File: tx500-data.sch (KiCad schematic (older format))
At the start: 52 parts, among them J1 USB_B_Micro, J2 CAT, J3 REM/DATA, J4 USB_A, U1 TUSB2036, U2 FT232RL, U3 HS-100B, U4 TPS76333, Y1 6MHz

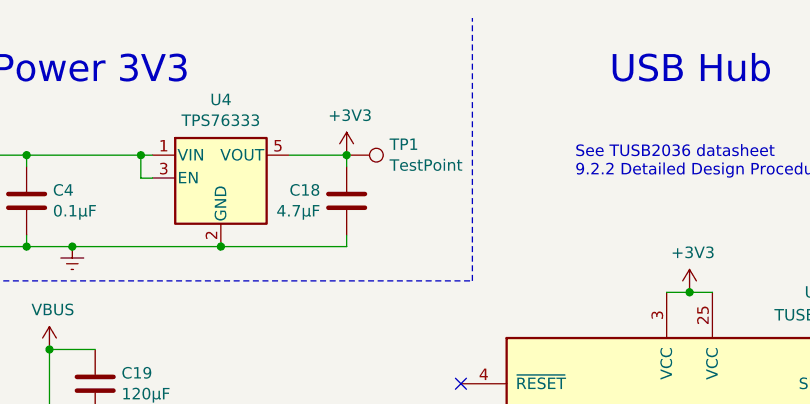
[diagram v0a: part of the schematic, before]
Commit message: Avoid schematic cross-junction
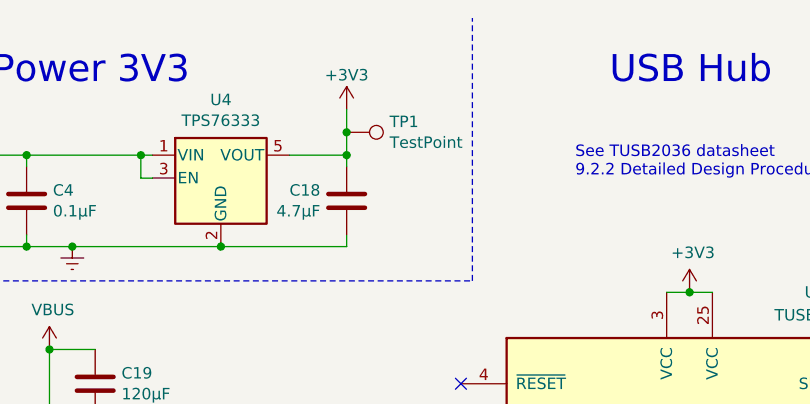
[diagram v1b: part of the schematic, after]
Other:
- moved on the sheet: TP1
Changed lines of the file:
@@
 L power:+3V3 #PWR0110
 U 1 1 60E968EB
-P 2800 1100
-F 0 "#PWR0110" H 2800 950 50  0001 C CNN
-F 1 "+3V3" H 2815 1273 50  0000 C CNN
-F 2 "" H 2800 1100 50  0001 C CNN
-F 3 "" H 2800 1100 50  0001 C CNN
-	1    2800 1100
+P 2800 900
+F 0 "#PWR0110" H 2800 750 50  0001 C CNN
+F 1 "+3V3" H 2800 1050 50  0000 C CNN
+F 2 "" H 2800 900 50  0001 C CNN
+F 3 "" H 2800 900 50  0001 C CNN
+	1    2800 900
 	1    0    0    -1
 $EndComp
@@
 L Connector:TestPoint TP1
 U 1 1 607EF82B
-P 2800 1100
-F 0 "TP1" V 2754 1288 50  0000 L CNN
-F 1 "TestPoint" V 2845 1288 50  0000 L CNN
-F 2 "TestPoint:TestPoint_Pad_D1.0mm" H 3000 1100 50  0001 C CNN
-F 3 "~" H 3000 1100 50  0001 C CNN
-	1    2800 1100
+P 2800 1000
+F 0 "TP1" V 2754 1188 50  0000 L CNN
+F 1 "TestPoint" V 2845 1188 50  0000 L CNN
+F 2 "TestPoint:TestPoint_Pad_D1.0mm" H 3000 1000 50  0001 C CNN
+F 3 "~" H 3000 1000 50  0001 C CNN
+	1    2800 1000
 	0    1    1    0
 $EndComp
@@
 $EndComp
 NoConn ~ 7900 5500
+Wire Wire Line
+	2800 1100 2800 1000
+Connection ~ 2800 1000
+Wire Wire Line
+	2800 1000 2800 900
 $EndSCHEMATC

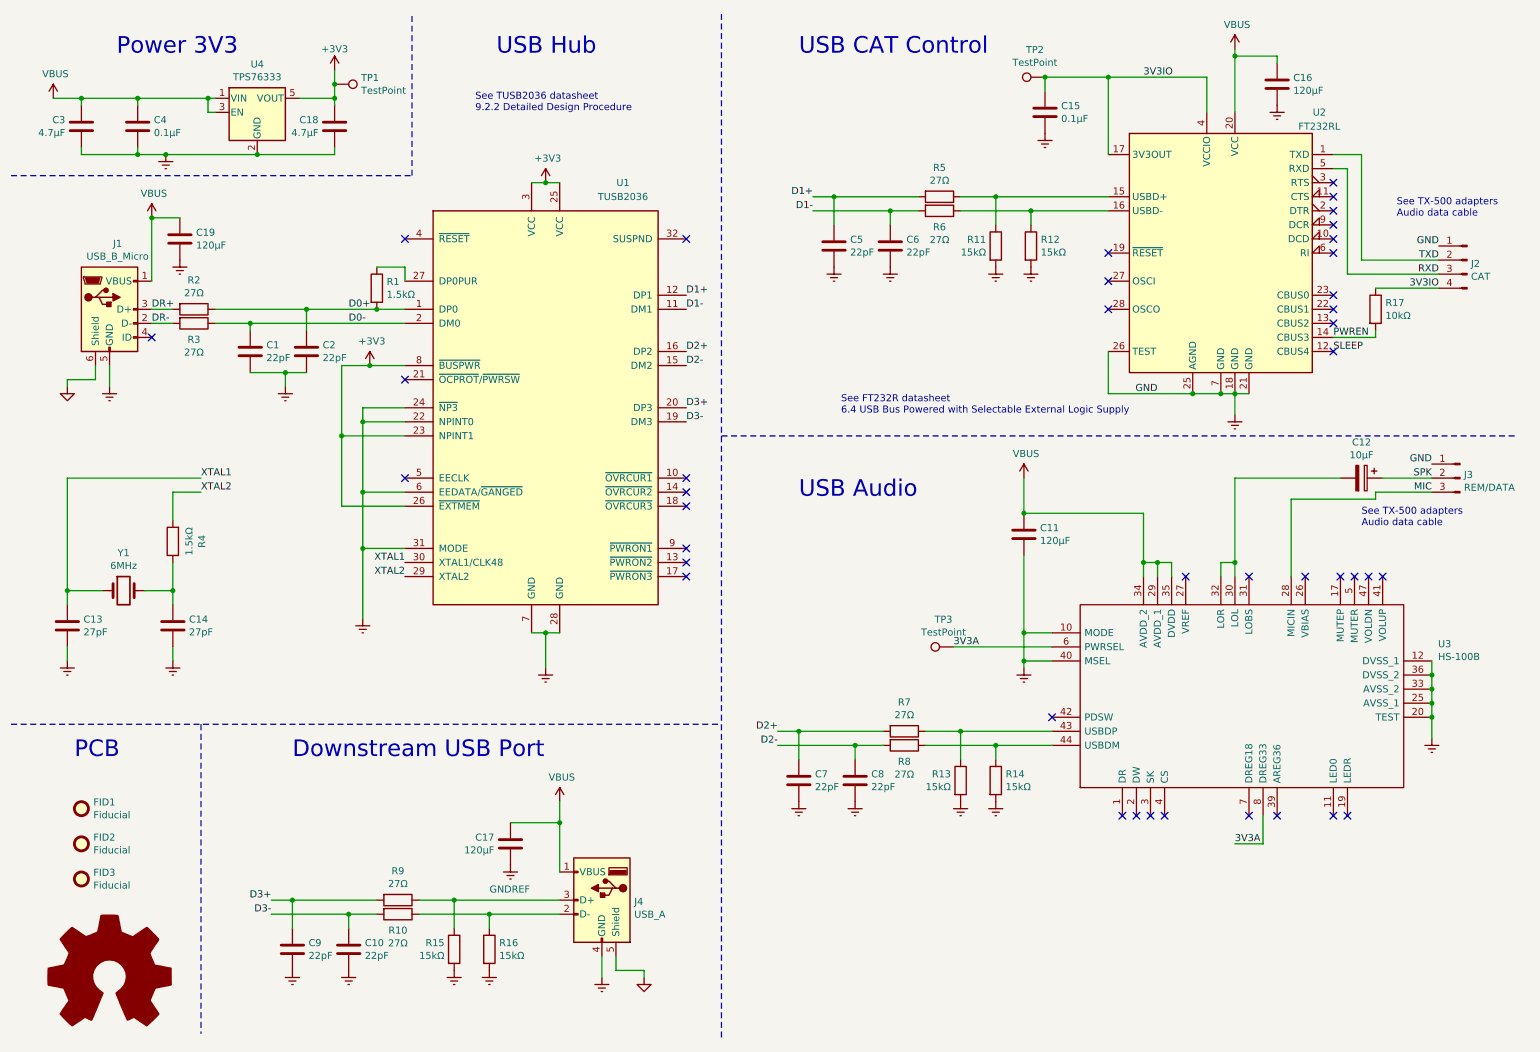
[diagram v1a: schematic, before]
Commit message: Add ESD and overcurrent protection
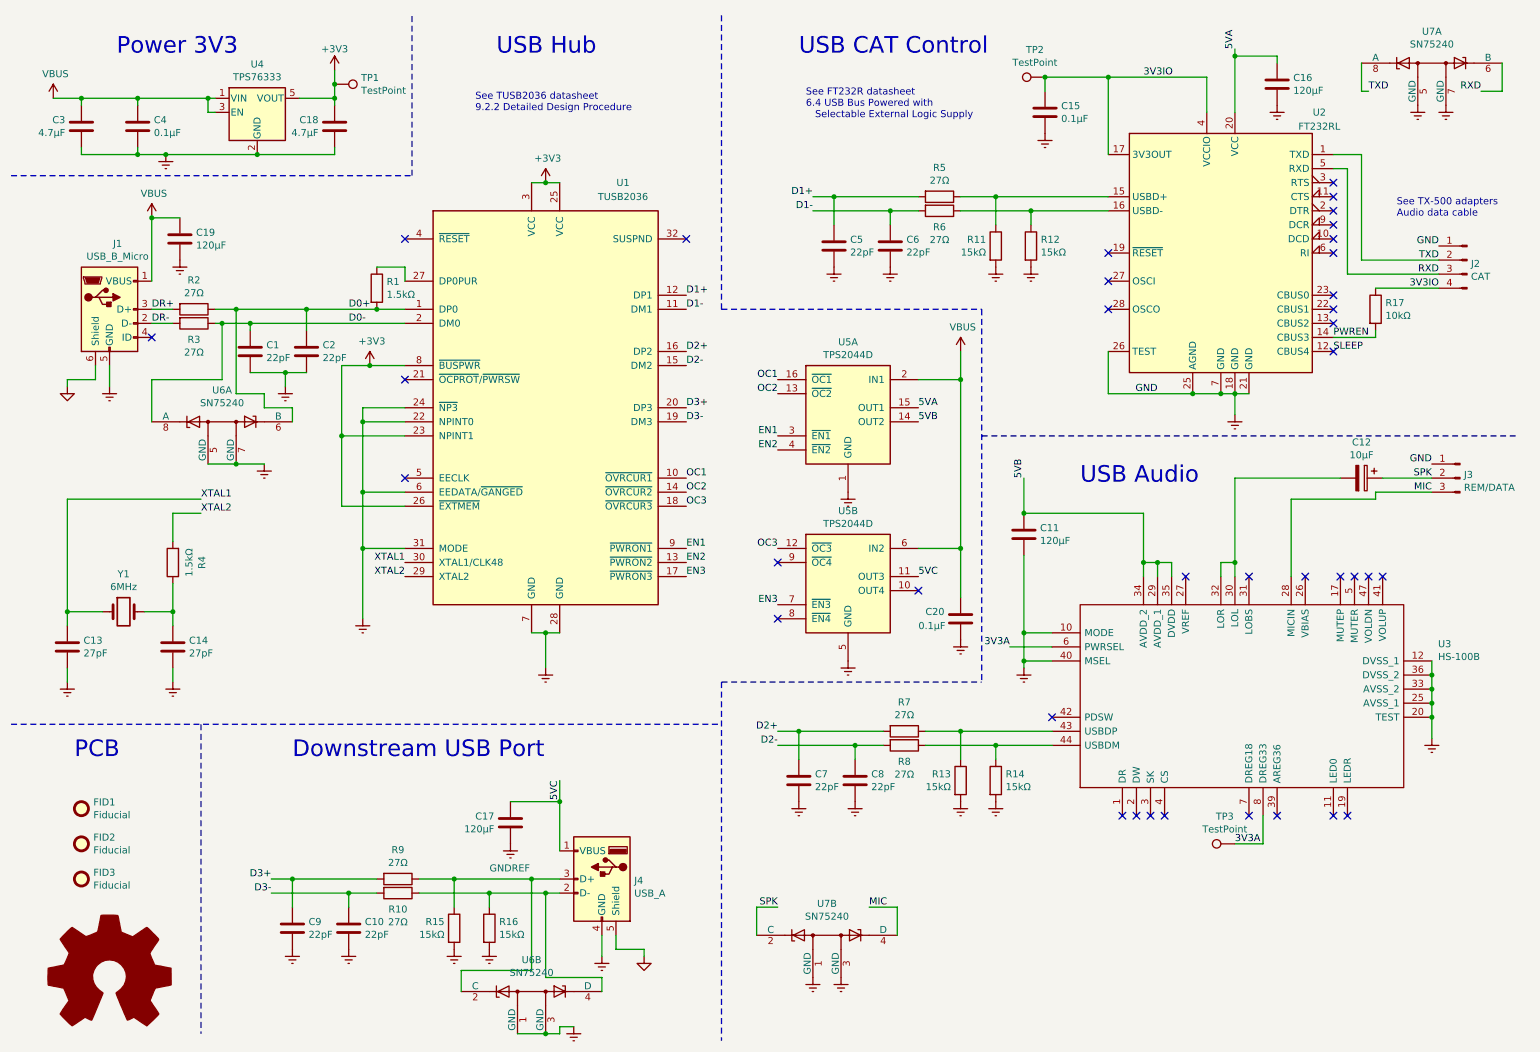
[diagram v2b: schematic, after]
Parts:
- added C20: 0.1μF, Capacitor_SMD:C_1210_3225Metric, symbol Device:C
- added U5: TPS2044D, Package_SO:SOIC-16_3.9x9.9mm_P1.27mm, symbol Power_Management:TPS2044D
- added U6, U7: SN75240, Package_SO:TSSOP-8_4.4x3mm_P0.65mm, symbol Power_Protection:SN75240
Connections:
- net D0+: now also U6.6 (B)
- net D0-: now also U6.8 (A)
- net GNDREF: now also C20.2, U5.1 (GND), U5.5 (GND), U6.1 (GND), U6.3 (GND), U6.5 (GND), U6.7 (GND), U7.1 (GND), U7.3 (GND), U7.5 (GND), U7.7 (GND)
- net MIC: now also U7.4 (D)
- net RXD: now also U7.6 (B)
- net SPK: now also U7.2 (C)
- net TXD: now also U7.8 (A)
- net VBUS: now also C20.1, U5.2 (IN1), U5.6 (IN2); no longer C11.1, C16.1, C17.1, J4.1 (VBUS), U2.20 (VCC), U3.29 (AVDD_1), U3.34 (AVDD_2), U3.35 (DVDD)
- net OC1: now reaches U1.10 (~OVRCUR1)
- net OC1: now also U5.16 (~OC1)
- net EN2: now reaches U1.13 (~PWRON2)
- net EN2: now also U5.4 (~EN2)
- net OC2: now reaches U1.14 (~OVRCUR2)
- net OC2: now also U5.13 (~OC2)
- net EN3: now reaches U1.17 (~PWRON3)
- net EN3: now also U5.7 (~EN3)
- net OC3: now reaches U1.18 (~OVRCUR3)
- net OC3: now also U5.12 (~OC3)
- net EN1: now reaches U1.9 (~PWRON1)
- net EN1: now also U5.3 (~EN1)
- net at J4.2 (D-), R10.1, R16.1: now also U6.4 (D)
- net at J4.3 (D+), R15.1, R9.1: now also U6.2 (C)
- new net 5VA: C16.1, U2.20 (VCC), U5.15 (OUT1)
- new net 5VB: C11.1, U3.29 (AVDD_1), U3.34 (AVDD_2), U3.35 (DVDD), U5.14 (OUT2)
- new net 5VC: C17.1, J4.1 (VBUS), U5.11 (OUT3)
- no-connect marks 40 -> 37
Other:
- note added: "See FT232R datasheet\n6.4 USB Bus Powered with \n Selectable External Logic Supply"
- note removed: "See FT232R datasheet\n6.4 USB Bus Powered with Selectable External Logic Supply"
- moved on the sheet: C10, C13, C14, C17, C9, J4, R10, R15, R16, R4, R9, TP3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

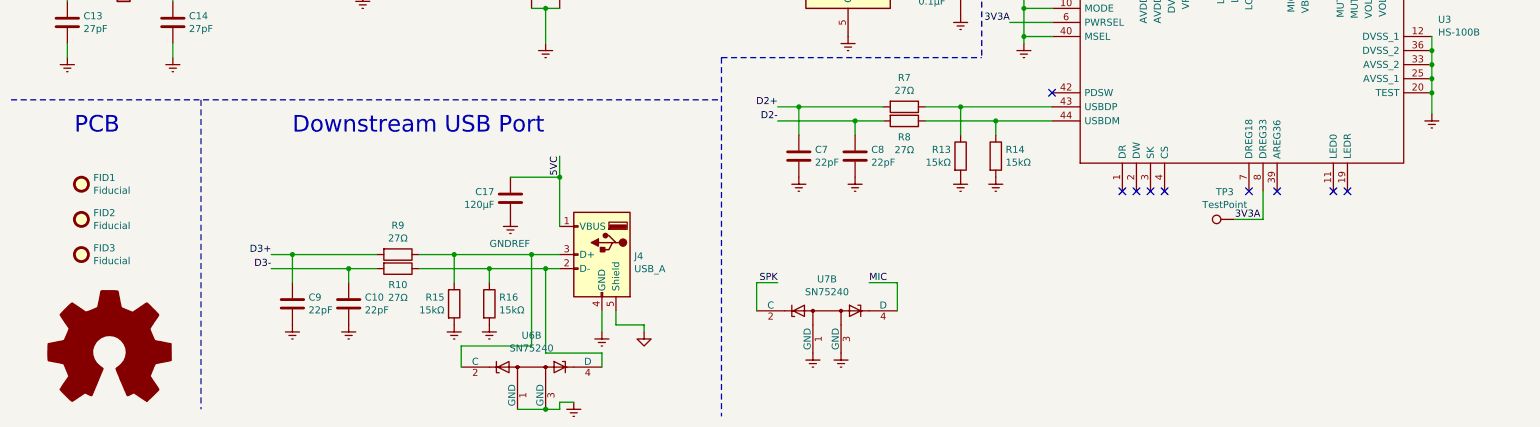
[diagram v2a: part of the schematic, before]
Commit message: Move 2mm away from enclosure sides
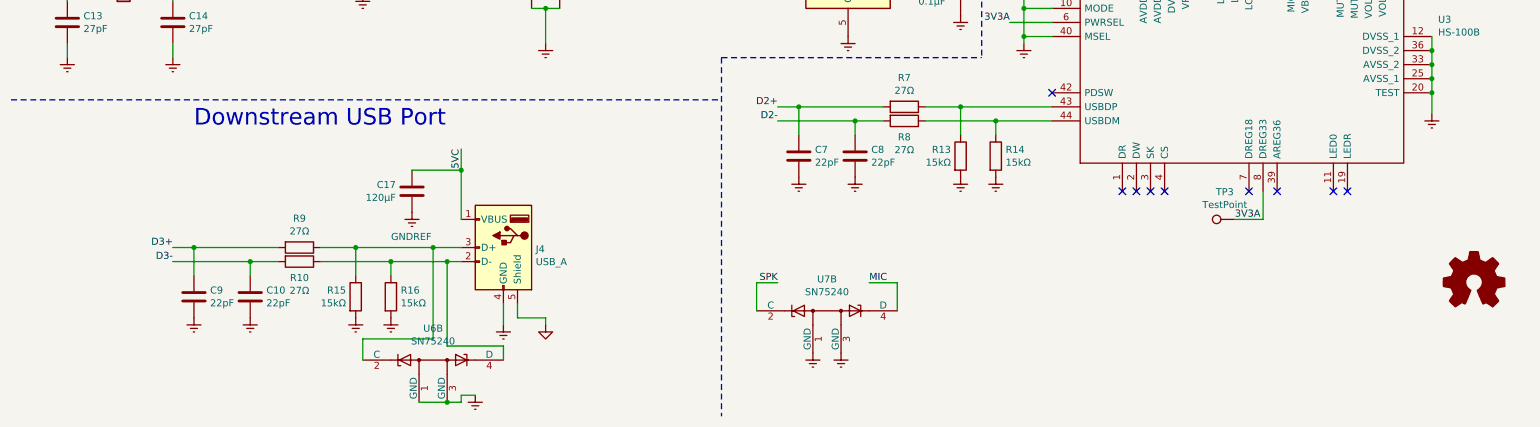
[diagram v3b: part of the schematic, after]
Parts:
- removed FID1, FID2, FID3: Fiducial, Fiducial:Fiducial_1mm_Mask2mm, symbol Mechanical:Fiducial
- removed LOGO1: Logo_Open_Hardware_Large, Symbol:OSHW-Logo2_9.8x8mm_Copper, symbol Graphic:Logo_Open_Hardware_Large
- added LOGO1: Logo_Open_Hardware_Small, Symbol:OSHW-Logo2_9.8x8mm_Copper, symbol Graphic:Logo_Open_Hardware_Small
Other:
- note removed: "PCB"
- moved on the sheet: C10, C17, C9, J4, R10, R15, R16, R9, U6B

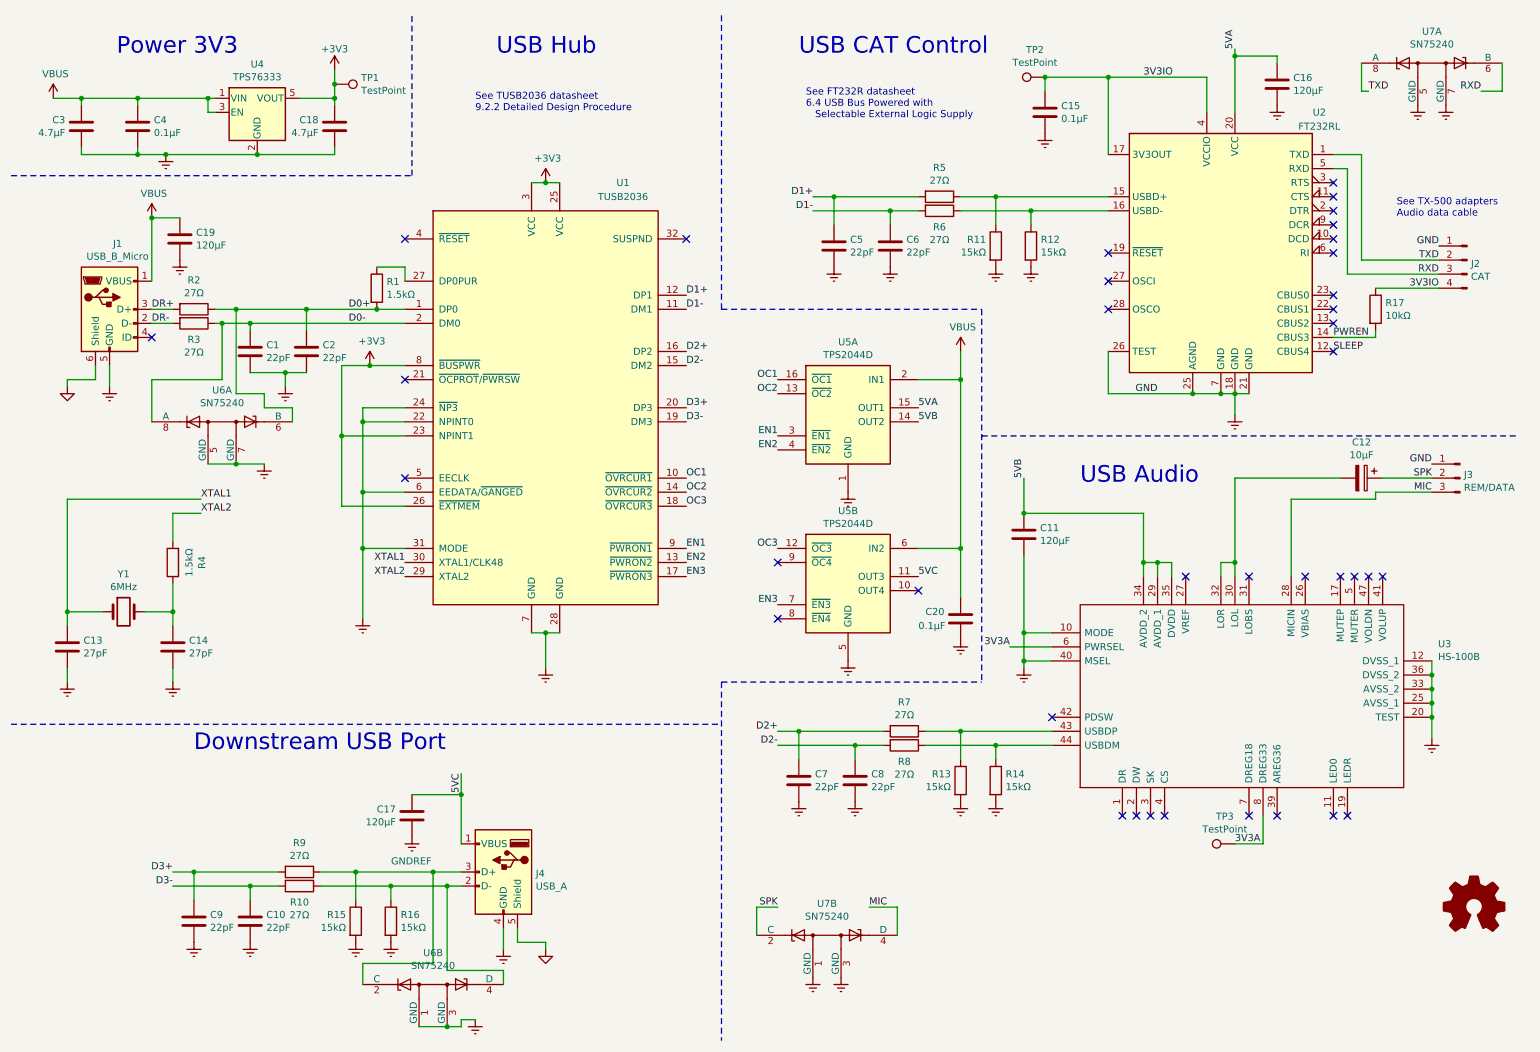
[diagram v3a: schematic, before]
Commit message: Incorporate advice
* Remove 120uF decoupling cap for J1
* Pull up EN4 to disable OUT4
* Add 0ohm resistors to L/R audio lines in case I need them
* Also, move components farther away from the enclosure edges
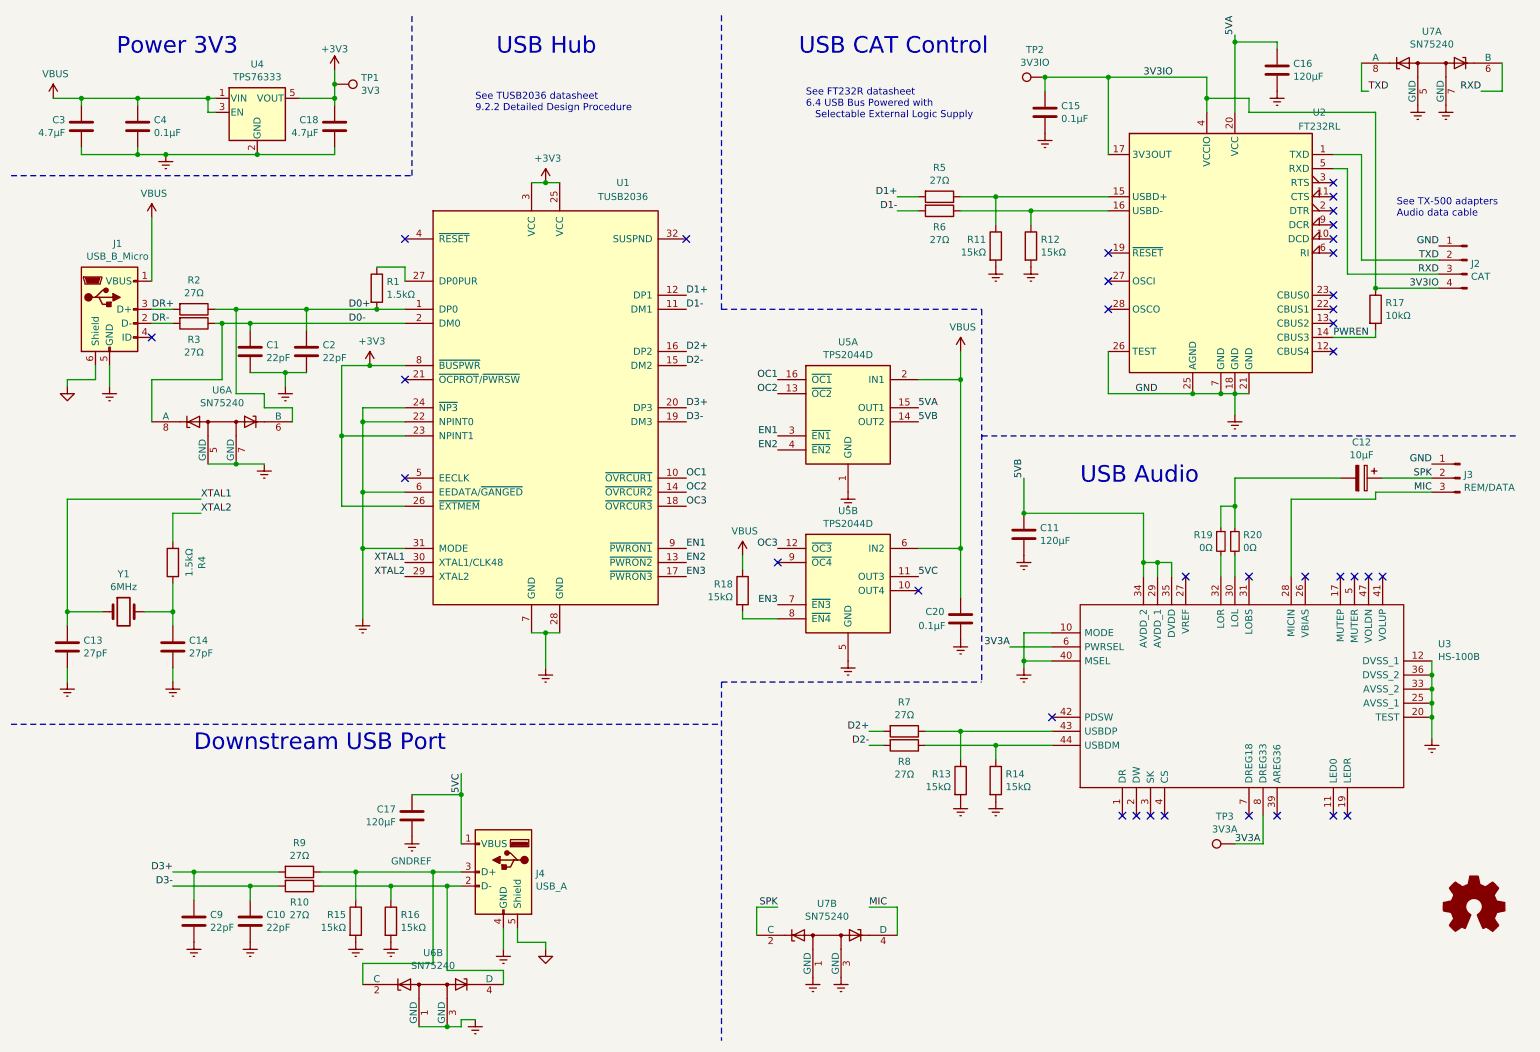
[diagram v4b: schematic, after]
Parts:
- removed C19: 120μF, Capacitor_SMD:C_1210_3225Metric, symbol Device:C
- removed C5, C6, C7, C8: 22pF, Capacitor_SMD:C_1210_3225Metric, symbol Device:C
- added R18: 15kΩ, Resistor_SMD:R_1210_3225Metric, symbol Device:R
- added R19, R20: 0Ω, Resistor_SMD:R_1210_3225Metric, symbol Device:R_Small
- TP1: value TestPoint -> 3V3
- TP2: value TestPoint -> 3V3IO
- TP3: value TestPoint -> 3V3A
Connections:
- net VBUS: now also R18.1
- net at U5.8 (~EN4): now also R18.2
- net SLEEP: no longer names the net of U2.12 (CBUS4)
- new net: C12.2, R19.1, R20.1
- new net: R20.2, U3.30 (LOL)
- new net: R19.2, U3.32 (LOR)
- no-connect marks 37 -> 36
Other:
- moved on the sheet: C16

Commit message: Add 3D models, and various cleanup
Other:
- moved on the sheet: C10, C17, C9, J4, R10, R15, R16, R9, U6B
